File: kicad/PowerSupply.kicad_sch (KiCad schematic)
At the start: 51 parts, among them Q1 FQP17P10, Q2 FQP17P10, Q3 NX138AKR, Q4 NX138AKR, U1 OPA4196

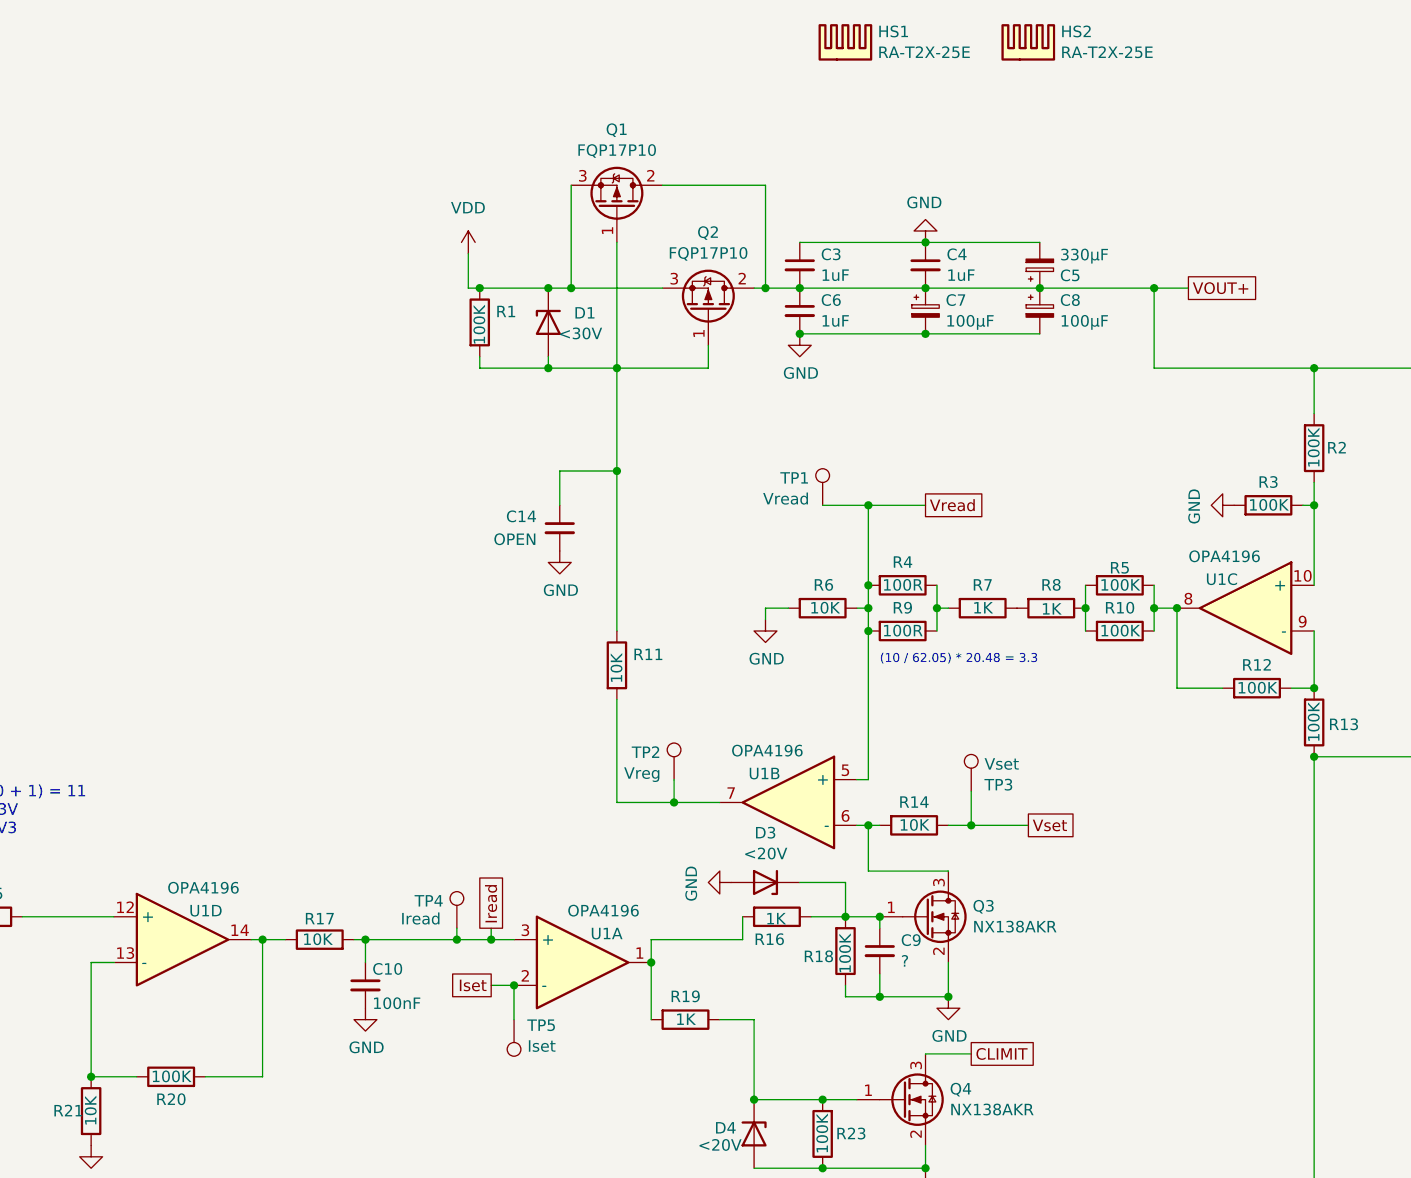
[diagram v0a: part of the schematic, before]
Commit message: Changes
- USB C connector
- 12V Buck converter instead of LM317
- Bunch of stuff I don't remember
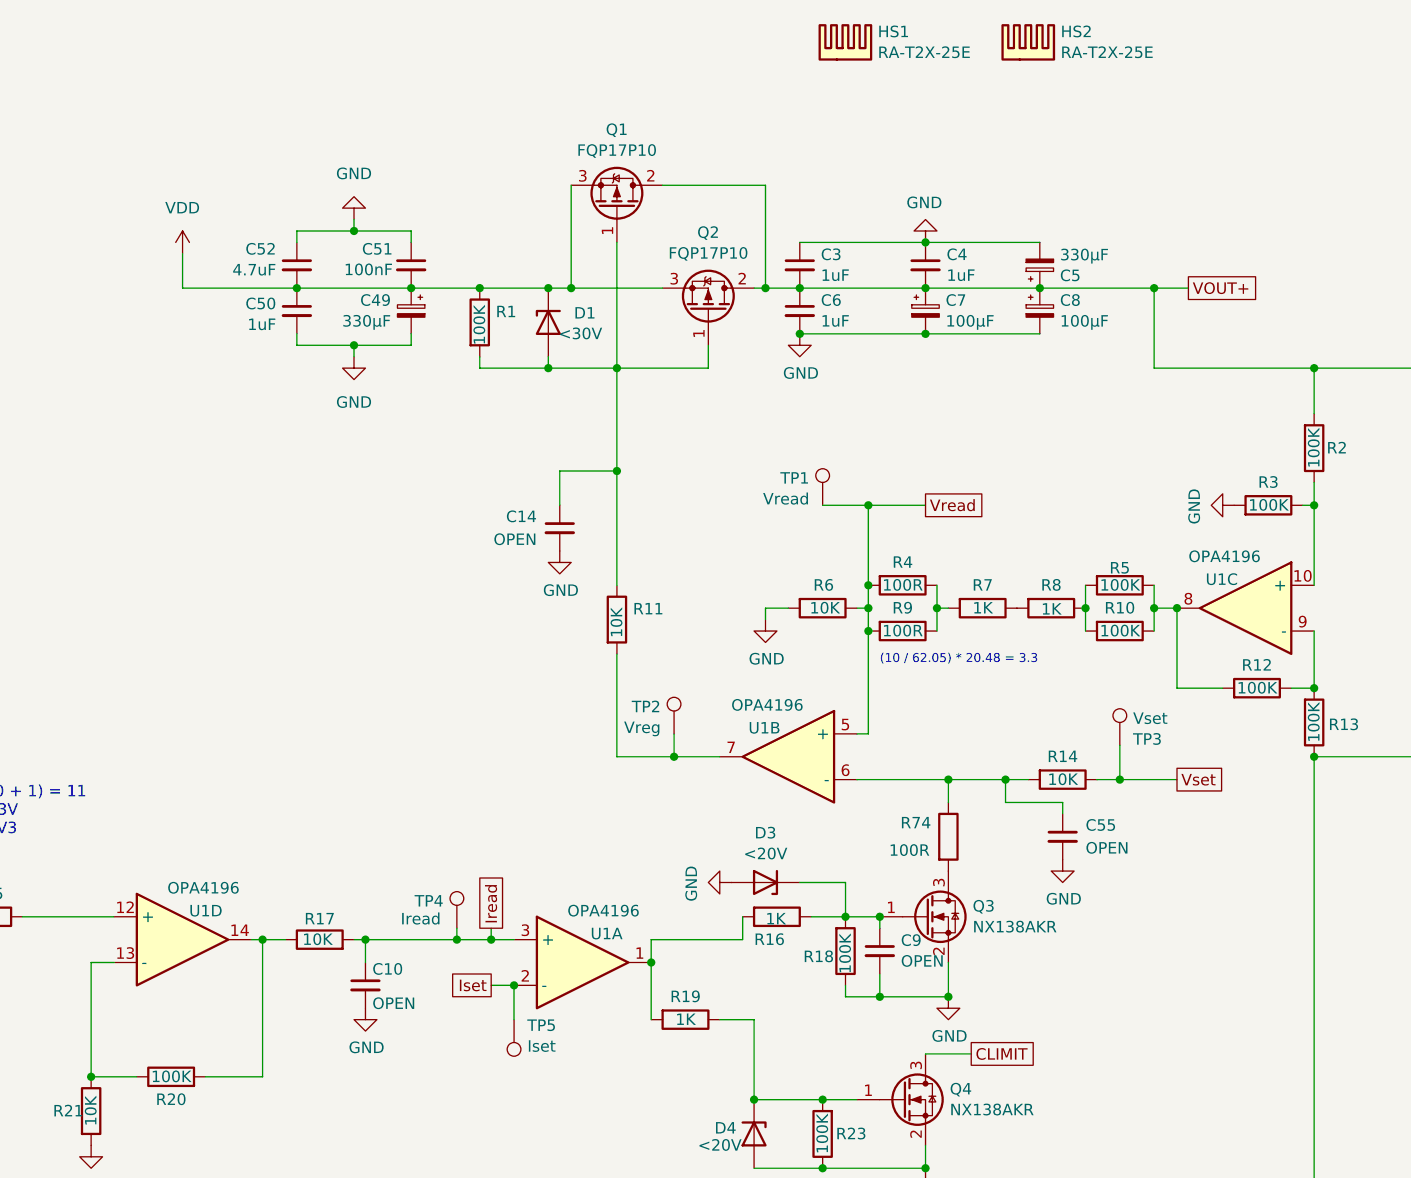
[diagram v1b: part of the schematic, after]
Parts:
- added C49: 330µF, Capacitor_THT:CP_Radial_D8.0mm_P3.50mm, symbol Device:C_Polarized_Small
- added C50: 1uF, Capacitor_SMD:C_0805_2012Metric_Pad1.18x1.45mm_HandSolder, symbol Device:C_Small
- added C51: 100nF, Capacitor_SMD:C_0805_2012Metric_Pad1.18x1.45mm_HandSolder, symbol Device:C_Small
- added C52: 4.7uF, Capacitor_SMD:C_0805_2012Metric_Pad1.18x1.45mm_HandSolder, symbol Device:C_Small
- added C55: OPEN, Capacitor_SMD:C_0805_2012Metric_Pad1.18x1.45mm_HandSolder, symbol Device:C_Small
- added R74: 100R, Resistor_SMD:R_0805_2012Metric_Pad1.20x1.40mm_HandSolder, symbol Device:R
- C10: value 100nF -> OPEN
- C14: footprint (none) -> Capacitor_SMD:C_0805_2012Metric_Pad1.18x1.45mm_HandSolder
- C9: value ? -> OPEN
- R11, R14, R17, R21, R6: MPN RC0805FR-1310KL -> RC0805FR-1310KL
- R15, R7, R8: MPN CRGCQ0805F100K -> RC0805FR-131KL
- R16: MPN (none) -> RC0805FR-131KL
- R19: MPN CRCW080510K0FKEAC -> RC0805FR-131KL
- R4, R9: MPN CRGCQ0805F100K -> RC0805FR-13100RL
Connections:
- net GND: now also C49.2, C50.2, C51.1, C52.1, C55.2
- net VDD: now also C49.1, C50.1, C51.2, C52.2
- net at R14.2, U1.6 (-): now also C55.1, R74.1; no longer Q3.3 (D)
- new net: Q3.3 (D), R74.2
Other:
- moved on the sheet: R11, R14, TP2, TP3, U1B

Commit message: Commit
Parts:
- C10: MPN CC0805KRX7R9BB104 -> (none)
- C3, C4, C50, C6: MPN CL21B105KBFNNNF -> CL21B105KBFNNNF
- D1: value <30V -> BZT52B12; MPN (none) -> BZT52B12
- D3, D4: value <20V -> BZT52B12; MPN (none) -> BZT52B12
- R15: value 1K -> 0R; MPN RC0805FR-131KL -> 0805W8J0000T5E
- R74: value 100R -> 0R; MPN RC0805FR-13100RL -> 0805W8J0000T5E
- TP1, TP2, TP3, TP4, TP5: now left out of the parts list
